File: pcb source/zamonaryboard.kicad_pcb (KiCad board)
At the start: 2 copper layers, 52.3 x 40.6 mm, 26 parts, among them J1 USB_C_Receptacle_USB2.0_14P, SW1 SW_Push, U1 ESP32-S2, U2 ME6211C33M5, Y1 Crystal_GND24

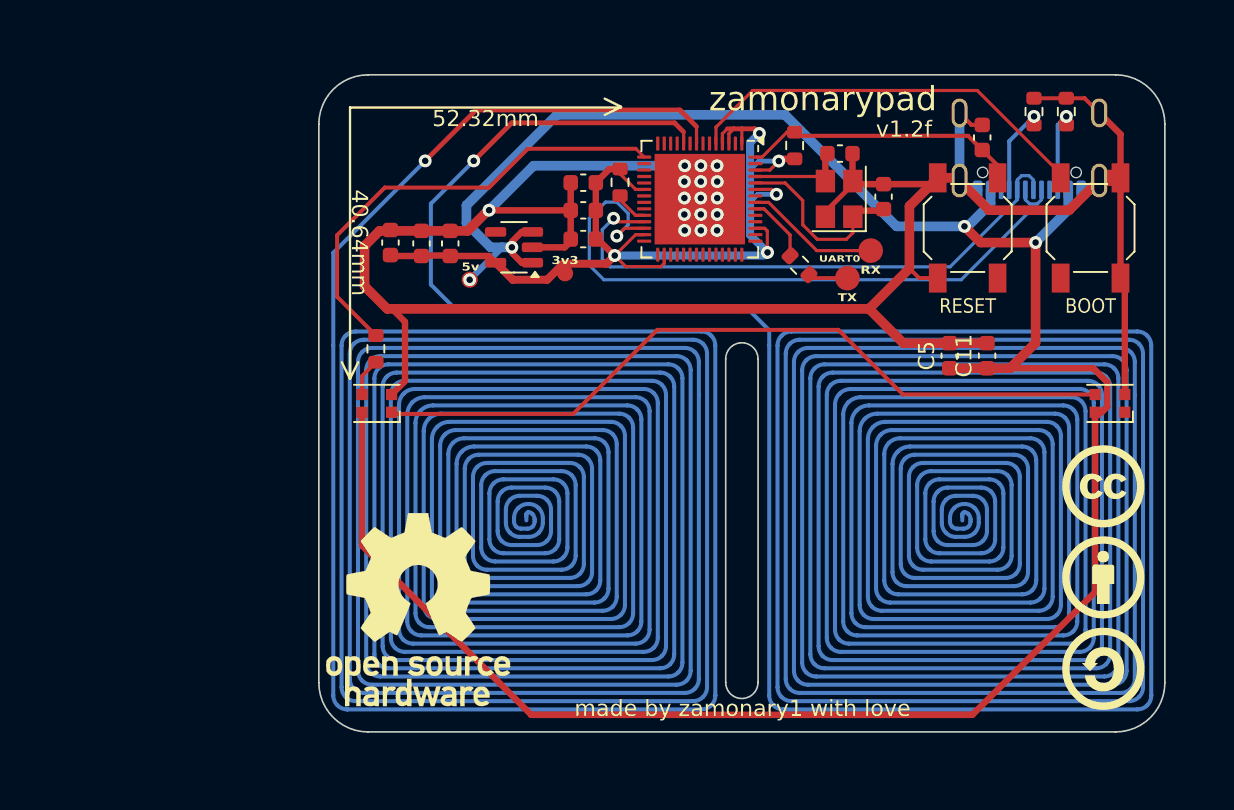
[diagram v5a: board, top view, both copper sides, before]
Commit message: Testing of auto-release of firmware
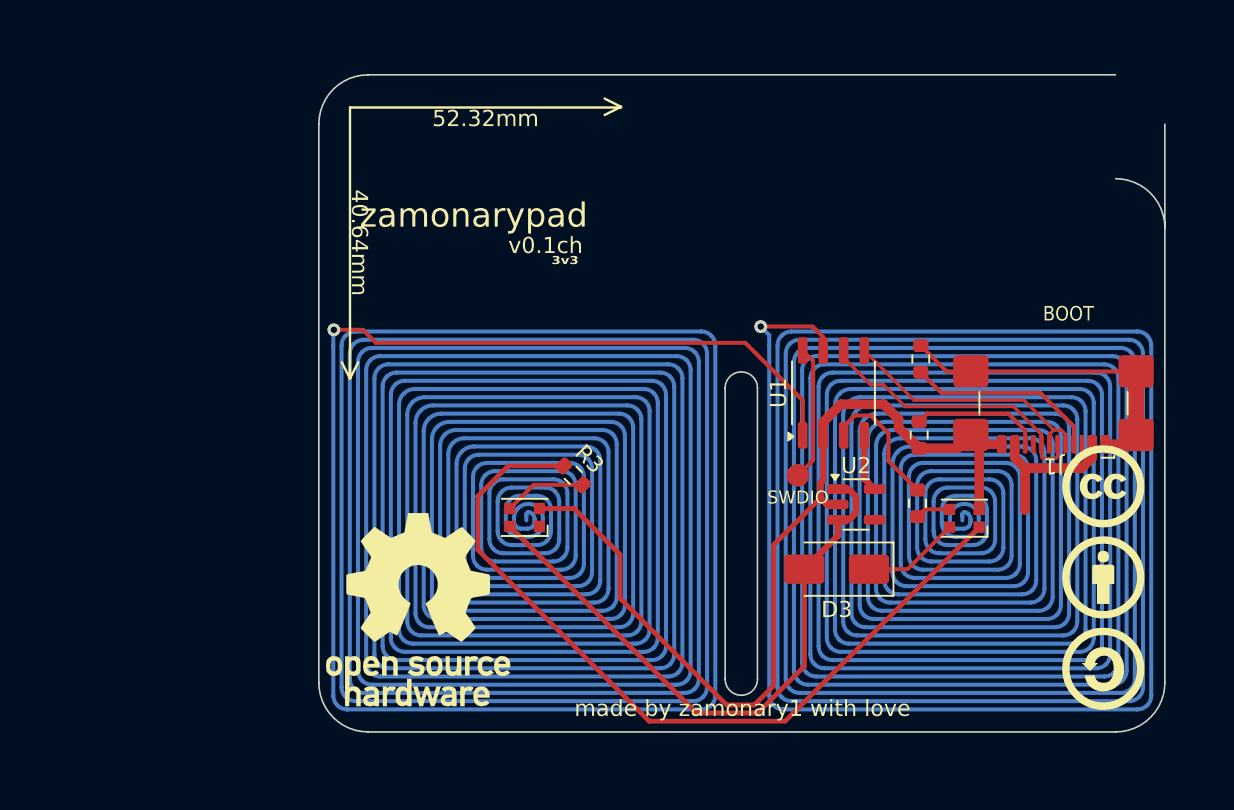
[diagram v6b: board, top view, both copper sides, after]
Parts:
- removed C1, C11, C4: 100nF, Capacitor_SMD:C_0603_1608Metric
- removed C10, C2, C5, C7: 1uF, Capacitor_SMD:C_0603_1608Metric
- removed C3: 10uF, Capacitor_SMD:C_0603_1608Metric
- removed C6: 100pF, Capacitor_SMD:C_0603_1608Metric
- removed C8, C9: 15pF, Capacitor_SMD:C_0603_1608Metric
- removed R4: 10K, Resistor_SMD:R_0603_1608Metric
- removed R5: 480, Resistor_SMD:R_0603_1608Metric
- removed SW-RST1, SW1: SW_Push, Button_Switch_SMD:SW_SPST_SKQG_WithoutStem
- removed Y1: Crystal_GND24, Crystal:Crystal_SMD_3225-4Pin_3.2x2.5mm
- added D3: US1B, Diode_SMD:D_SMA, F.Cu at (150.9, 102.2)
- J1: footprint Connector_USB:USB_C_Receptacle_GCT_USB4105-xx-A_16P_TopMnt_Horizontal -> Connector_USB:USB_C_Receptacle_GCT_USB4110; moved to F.Cu
- R3: value 10K -> 480
- U1: value ESP32-S2 -> CH32V003JxMx; footprint Package_DFN_QFN:QFN-56-1EP_7x7mm_P0.4mm_EP5.6x5.6mm -> Package_SO:SOP-8_3.9x4.9mm_P1.27mm
- moved R6 34.8 mm to (155.9, 98.1)
- moved U2 26.5 mm to (152.1, 98.2), turned to 0 degrees
- moved R3 24.6 mm to (134.6, 96.4), turned to -45 degrees
- moved R2 22.0 mm to (156.0, 93.9), turned to 90 degrees
- moved R1 16.8 mm to (156.1, 89.2)
- moved J1 15.8 mm to (164.3, 90.8), turned to 180 degrees
- moved U1 14.6 mm to (150.7, 91.3), turned to 90 degrees
- moved D2 11.5 mm to (131.6, 99.0)
- moved D1 11.5 mm to (158.8, 99.0)
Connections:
- D1 pad 1: unconnected-(D1-DOUT-Pad1) -> Net-(D1-DOUT)
- D1 pad 4: VBUS -> Net-(D1-VDD)
- D2 pad 1: Net-(D1-DIN) -> unconnected-(D2-DOUT-Pad1)
- R3 pad 1: Net-(U1-CHIP_PU/RESET) -> Net-(D1-DOUT)
- R3 pad 2: +3V3 -> Net-(D2-DIN)
- R6 pad 2: Net-(D2-DIN) -> Net-(D1-DIN)
- U1 pad 1: +3V3 -> BTN1
- U1 pad 2: unconnected-(U1-LNA_IN/RF-Pad2) -> GND
- U1 pad 3: +3V3 -> aRGB_pin
- U1 pad 5: Net-(U1-GPIO0/BOOT) -> D-
- U1 pad 6: unconnected-(U1-GPIO1/ADC1_CH0-Pad6) -> D+
- U1 pad 7: unconnected-(U1-GPIO2/ADC1_CH1-Pad7) -> BTN2
- U1 pad 8: BTN1 -> SWD
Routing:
- net VBUS: track 152.1 -> 47.3 mm, vias 4 -> 0
- net GND: track 148.0 -> 77.8 mm, vias 16 -> 0
- net +3V3: track 63.3 -> 3.59 mm, vias 5 -> 0
- net Net-(D1-DOUT): track 0.00 -> 49.8 mm
- net Net-(D1-DIN): track 47.7 -> 2.17 mm
- net BTN2: track 1144.2 -> 1103.8 mm
- net Net-(U1-GPIO0/BOOT): track 25.7 -> 0.00 mm
- net D+: track 42.0 -> 17.9 mm, vias 1 -> 0
- net aRGB_pin: track 28.6 -> 8.30 mm
- net D-: track 35.4 -> 16.2 mm, vias 1 -> 0
- net Net-(U1-CHIP_PU/RESET): track 17.3 -> 0.00 mm
- net Net-(U1-XTAL_N): track 11.0 -> 0.00 mm
- net SWD: track 0.00 -> 8.38 mm
- net RX: track 8.37 -> 0.00 mm
- net Net-(J1-CC1): track 5.17 -> 12.0 mm, vias 1 -> 0
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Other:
- outline, holes or cut-outs redrawn
- board text added: "SWDIO"
- board text added: "v0.1ch"
- board text removed: "5v"
- board text removed: "RESET"
- board text removed: "RX"
- board text removed: "TX"
- board text removed: "UART0"
- board text removed: "v1.2f"

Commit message: Working pcb
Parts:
- moved D3 5.60 mm to (156.5, 102.0), turned to 0 degrees
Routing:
- net VBUS: track 47.3 -> 62.8 mm
- net GND: track 77.8 -> 86.4 mm
- net Net-(D1-DOUT): track 49.8 -> 54.2 mm
- net Net-(D1-VDD): track 6.06 -> 4.38 mm
- net BTN2: track 1103.8 -> 1102.8 mm
- net BTN1: track 1131.4 -> 1130.9 mm
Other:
- board size 52.3 x 40.6 mm -> 52.2 x 24.8 mm
- board text removed: "3v3"
- board text removed: "BOOT"
